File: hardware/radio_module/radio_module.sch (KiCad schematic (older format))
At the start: 1 part, among them U8 conn2x18pcie

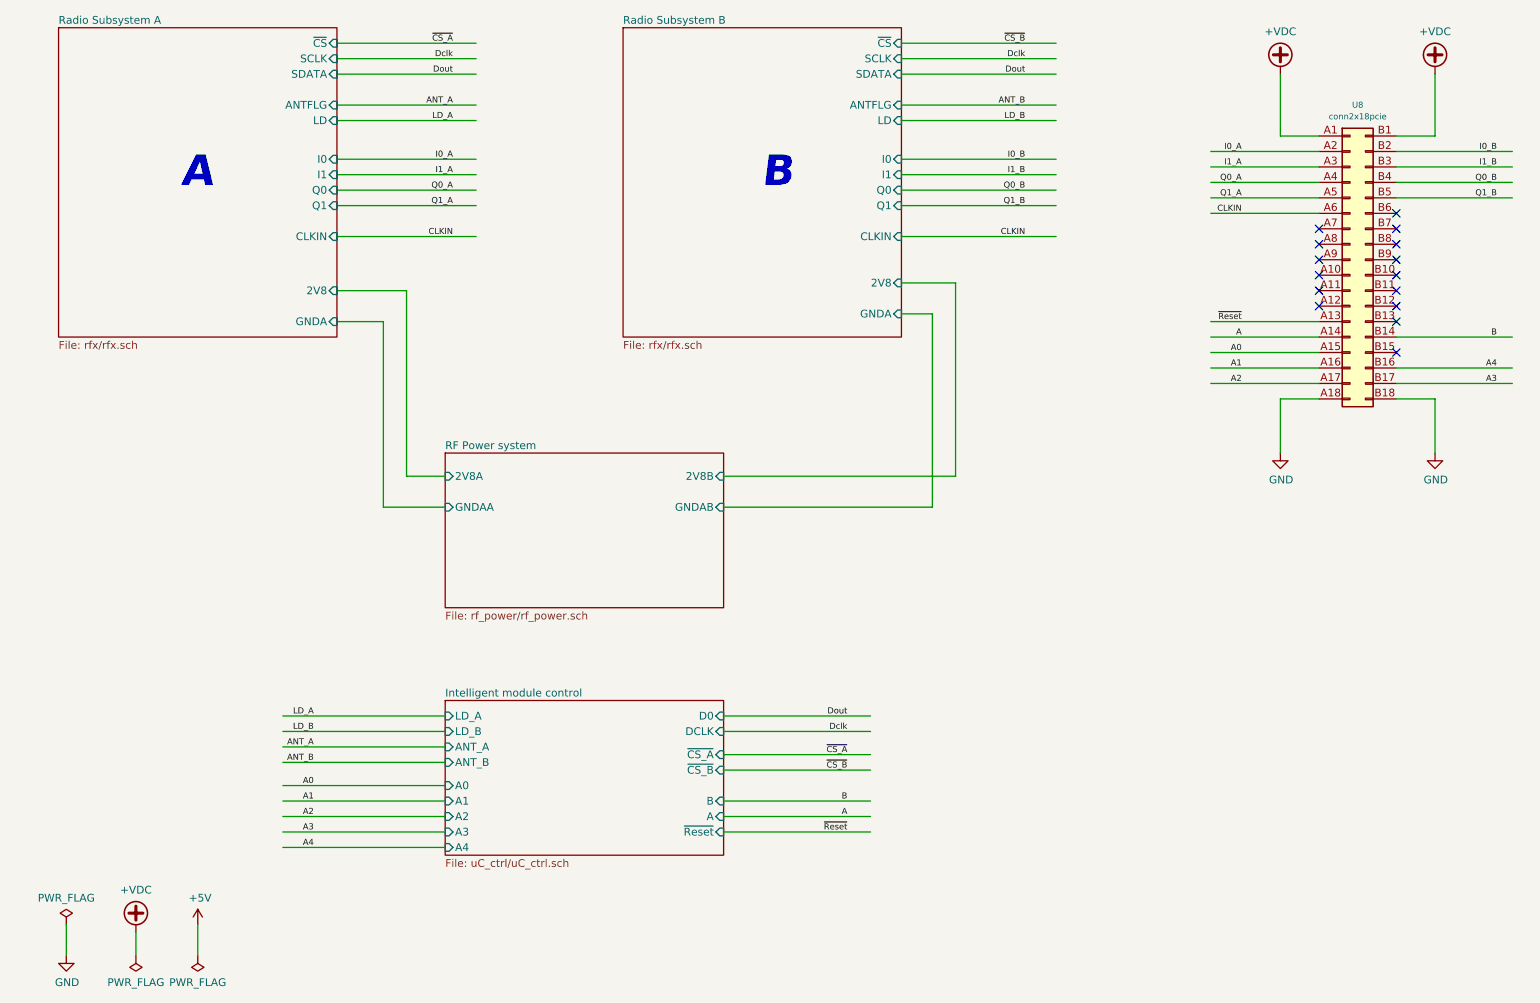
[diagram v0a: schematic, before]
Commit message: Initial complete layout of the radio board
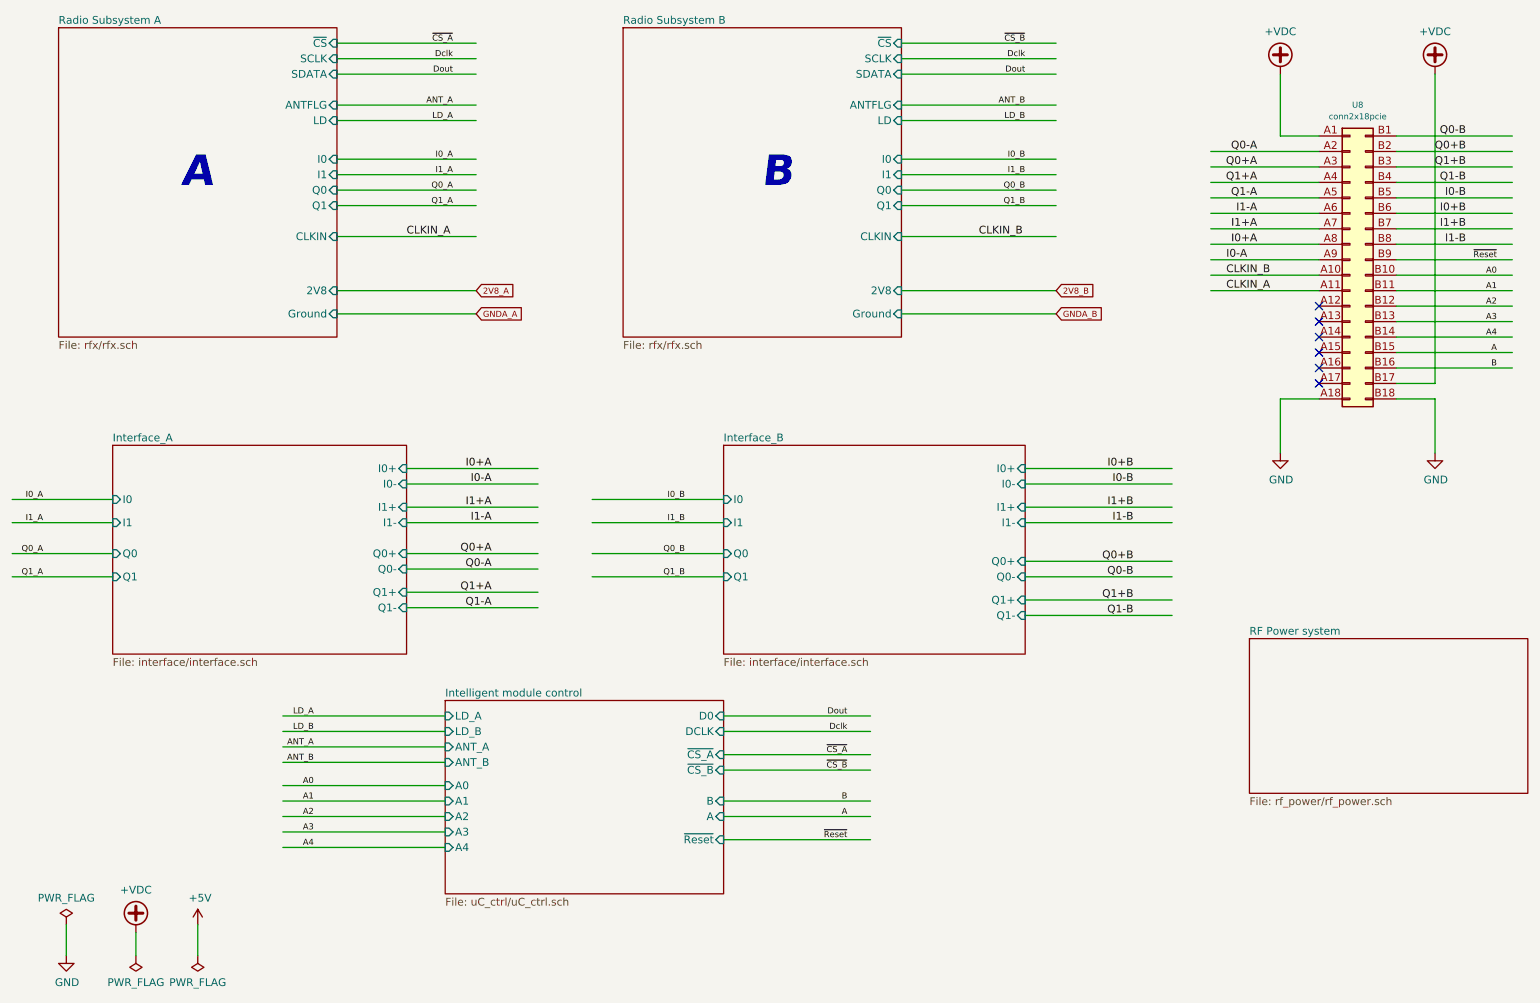
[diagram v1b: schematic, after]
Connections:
- net labels added: 2V8_A, 2V8_B, CLKIN_A, CLKIN_B, GNDA_A, GNDA_B, I0+A, I0+B, I0-A, I0-B, I1+A, I1+B, I1-A, I1-B, Q0+A, Q0+B, Q0-A, Q0-B, Q1+A, Q1+B, Q1-A, Q1-B
- net labels removed: CLKIN
- wire segments 76 -> 101
- no-connect marks 15 -> 6

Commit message: Update radio board, change crystal and get 3d up to date
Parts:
- added H1: MountingHole, MountingHole:MountingHole_3.2mm_M3, symbol Mechanical:MountingHole
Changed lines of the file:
@@
 Text Label 3400 2550 0    50   ~ 0
 CLKIN_A
+$Comp
+L Mechanical:MountingHole H1
+U 1 1 5DA919FC
+P 2550 7250
+F 0 "H1" H 2650 7296 50  0000 L CNN
+F 1 "MountingHole" H 2650 7205 50  0000 L CNN
+F 2 "MountingHole:MountingHole_3.2mm_M3" H 2550 7250 50  0001 C CNN
+F 3 "~" H 2550 7250 50  0001 C CNN
+	1    2550 7250
+	1    0    0    -1
+$EndComp
+Text Notes 2550 4750 2    197  Italic 39
+A
+Text Notes 6600 4700 2    197  Italic 39
+B
 $EndSCHEMATC

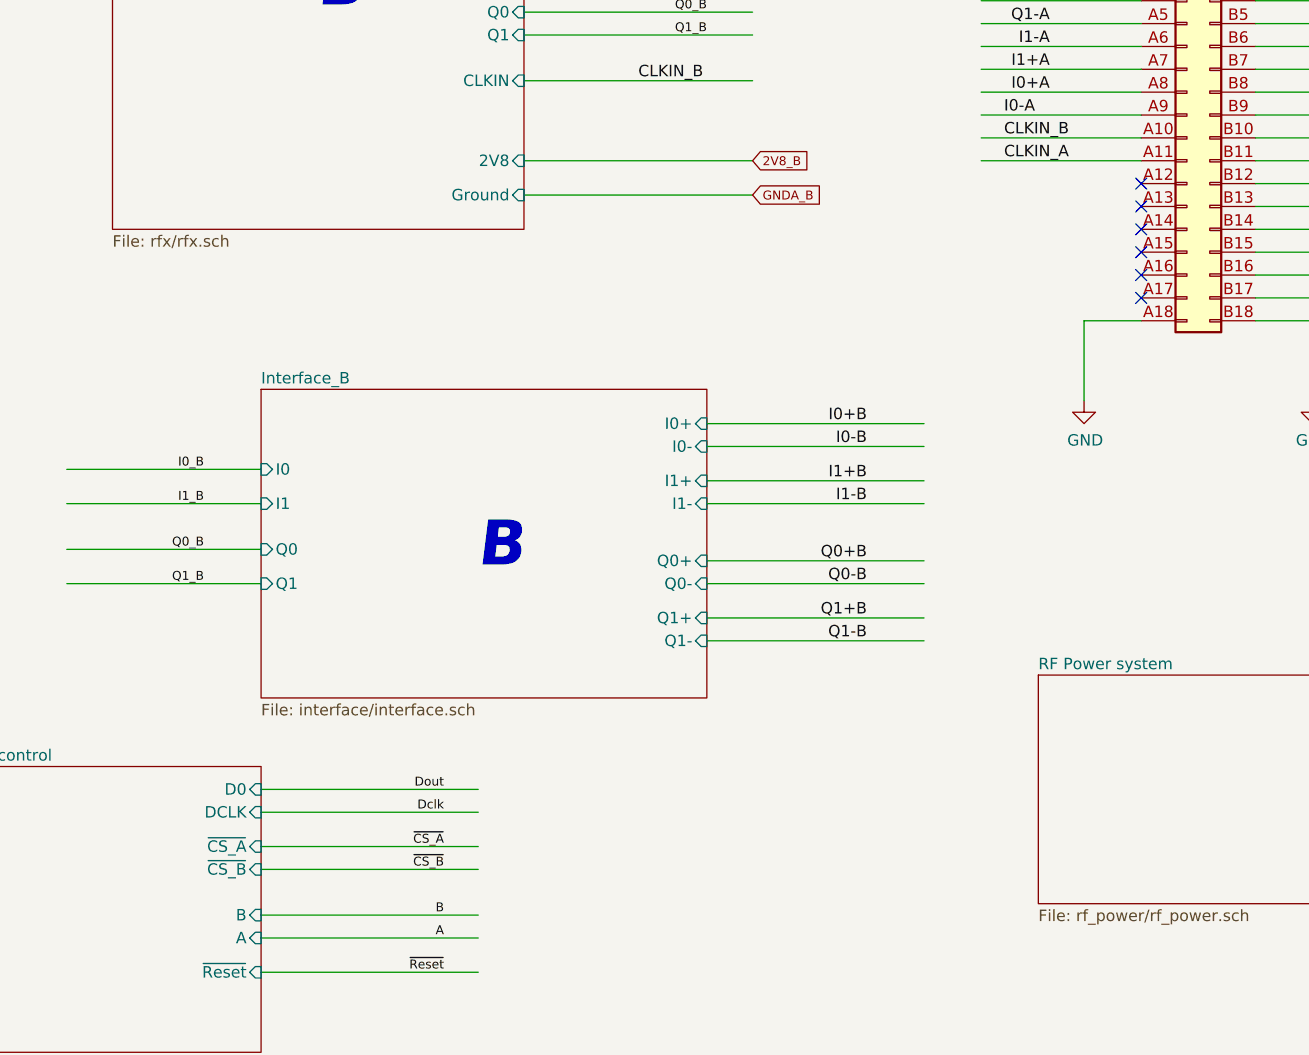
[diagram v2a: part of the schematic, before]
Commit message: Add Arduino programming lines. Tidy up layout
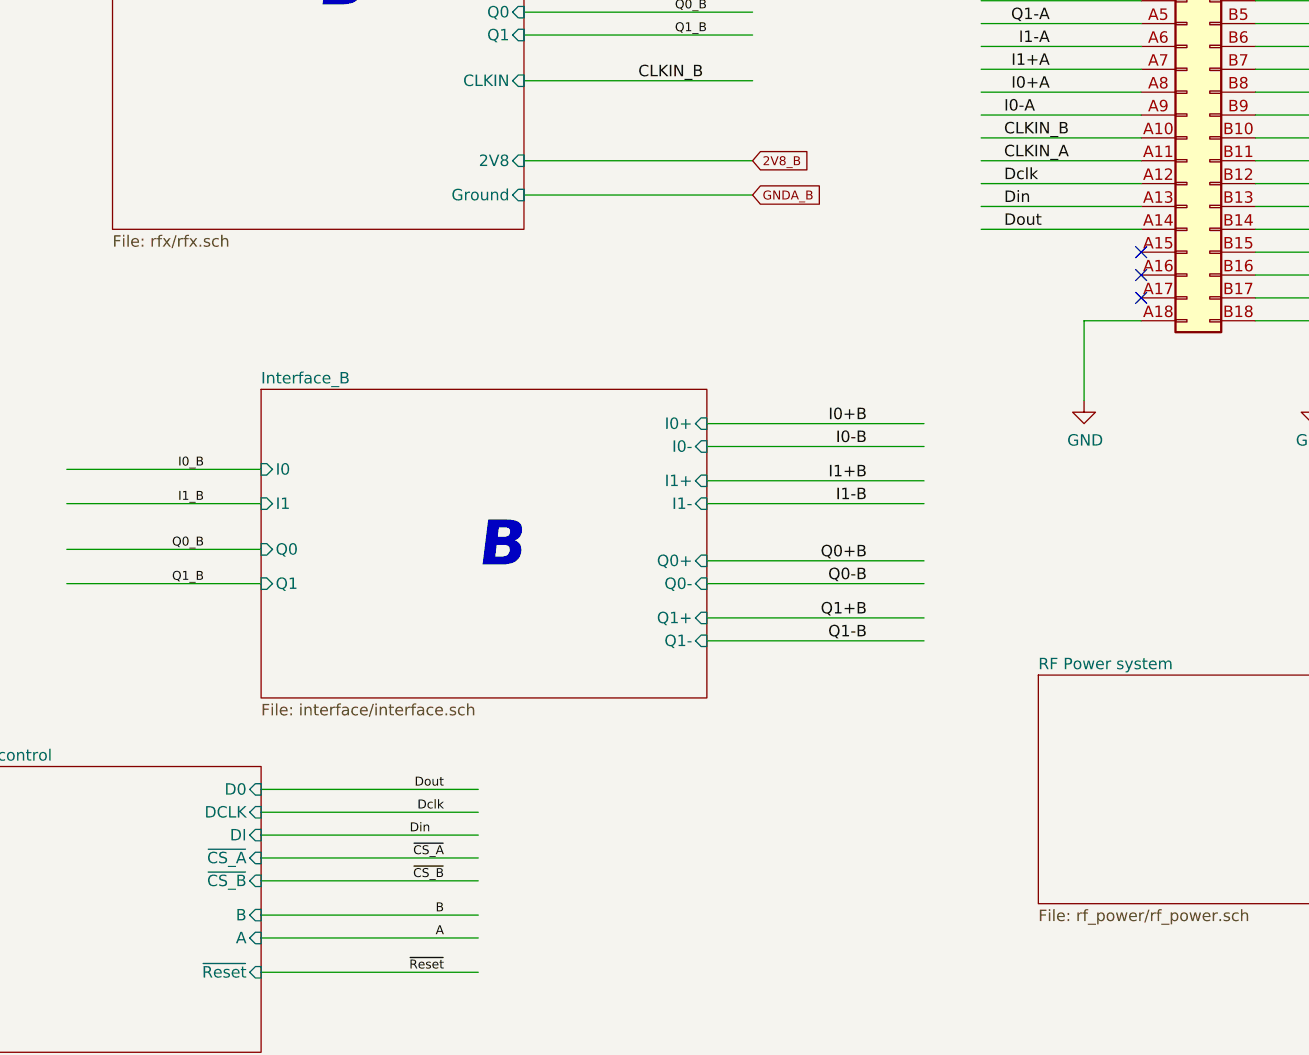
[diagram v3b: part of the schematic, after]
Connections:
- net labels added: Din
- wire segments 101 -> 105
- no-connect marks 6 -> 3
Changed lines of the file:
@@
 F11 "ANT_A" I L 3650 5850 50
 F12 "ANT_B" I L 3650 5950 50
-F13 "~CS_A" I R 5450 5900 50
-F14 "~CS_B" I R 5450 6000 50
+F13 "~CS_A" I R 5450 5950 50
+F14 "~CS_B" I R 5450 6050 50
 F15 "B" I R 5450 6200 50
 F16 "A" I R 5450 6300 50
 F17 "~Reset" I R 5450 6450 50
+F18 "DI" I R 5450 5850 50
 $EndSheet
 $Sheet
@@
 	5450 5750 6400 5750
 Wire Wire Line
-	5450 5900 6400 5900
-Wire Wire Line
-	5450 6000 6400 6000
+	5450 5950 6400 5950
+Wire Wire Line
+	5450 6050 6400 6050
 Wire Wire Line
 	5450 6200 6400 6200
@@
 Text Label 6250 5750 2    39   ~ 0
 Dclk
-Text Label 6250 5900 2    39   ~ 0
+Text Label 6250 5950 2    39   ~ 0
 ~CS_A
-Text Label 6250 6000 2    39   ~ 0
+Text Label 6250 6050 2    39   ~ 0
 ~CS_B
 Text Label 6250 6200 2    39   ~ 0
@@
 Text Label 10450 3200 2    39   ~ 0
 A4
-NoConn ~ 9300 3000
 Wire Wire Line
 	5450 6450 6400 6450
@@
 Text Label 10450 2700 2    39   ~ 0
 ~Reset
-NoConn ~ 9300 3100
-NoConn ~ 9300 3200
 NoConn ~ 9300 3300
 NoConn ~ 9300 3400
@@
 Text Notes 6600 4700 2    197  Italic 39
 B
+Wire Wire Line
+	5450 5850 6400 5850
+Text Label 6100 5850 0    39   ~ 0
+Din
+Wire Wire Line
+	9300 3100 8600 3100
+Wire Wire Line
+	9300 3200 8600 3200
+Wire Wire Line
+	9300 3000 8600 3000
+Text Label 8700 3100 0    50   ~ 0
+Din
+Text Label 8700 3200 0    50   ~ 0
+Dout
+Text Label 8700 3000 0    50   ~ 0
+Dclk
 $EndSCHEMATC
